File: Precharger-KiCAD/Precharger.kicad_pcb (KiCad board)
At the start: 2 copper layers, 42 parts, among them J1 Connector_Screw_Terminal_01x05, J2 Anderson_PP45_Power_RA, J3 Anderson_PP45_Power_RA, M1 Anderson_PP45_Staple_Nx2, M2 Anderson_PP45_Staple_Nx2, Q1 SQJQ480E, U1 MCP6001-OT, U2 MCP6001-OT, U3 R-78HE5.0-0.3, U4 CPC1004N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

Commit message: Continuing
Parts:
- added C6: 100nF, Capacitor_SMD:C_0805_2012Metric_Pad1.15x1.40mm_HandSolder, F.Cu at (120.6, 123.3)
- added D1: ASMB-MTB1-0A3A2, LED_SMD:LED_Avago_PLCC4_3.2x2.8mm_CW, F.Cu at (120.4, 97.9)
- added R11: 150R, Resistor_SMD:R_0805_2012Metric_Pad1.15x1.40mm_HandSolder, F.Cu at (122.5, 104.3)
- added R12: 100R, Resistor_SMD:R_0805_2012Metric_Pad1.15x1.40mm_HandSolder, F.Cu at (120.0, 104.3)
- added R13: 100R, Resistor_SMD:R_0805_2012Metric_Pad1.15x1.40mm_HandSolder, F.Cu at (117.6, 104.3)
- J1: value Connector_Screw_Terminal_01x05 -> Screw_Terminal_01x04; footprint Connector_Phoenix_MC:PhoenixContact_MCV_1,5_5-G-3.5_1x05_P3.50mm_Vertical -> TerminalBlock_Phoenix:TerminalBlock_Phoenix_PT-1,5-4-3.5-H_1x04_P3.50mm_Horizontal
- U4: moved to F.Cu
- moved R1 123.4 mm to (196.3, 73.9), turned to 270 degrees
- moved C4 106.8 mm to (189.8, 105.4)
- moved TP3 94.2 mm to (191.3, 97.8)
- moved R2 82.8 mm to (196.3, 78.2), turned to 270 degrees
- moved TP4 81.7 mm to (190.9, 133.8)
- moved U4 78.2 mm to (158.7, 61.7)
- moved JP6 75.9 mm to (160.5, 135.4)
- moved JP7 74.7 mm to (190.1, 125.7)
- moved JP5 74.0 mm to (160.5, 132.9)
- moved C1 73.8 mm to (185.1, 66.0)
- moved J3 73.8 mm to (121.3, 68.0)
- moved Q1 73.8 mm to (127.3, 76.3)
- moved A1 73.8 mm to (169.0, 97.8)
- moved C2 73.8 mm to (178.1, 69.7)
- moved C3 73.8 mm to (178.4, 73.7)
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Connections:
- A1 pad 12: Net-(A1-Pad12) -> /LED_R
- A1 pad 13: Net-(A1-Pad13) -> /LED_G
- A1 pad 14: Net-(A1-Pad14) -> /LED_B
- A1 pad 29: Net-(A1-Pad29) -> GND
- A1 pad 4: Net-(A1-Pad4) -> GND
- J1 pad 1: Net-(J1-Pad1) -> /ISO_GND
- J1 pad 2: Net-(J1-Pad2) -> /ISO_TX
- J1 pad 3: Net-(J1-Pad3) -> /ISO_RX
- J1 pad 4: Net-(J1-Pad4) -> /ISO_VCC
- JP5 pad 2: Net-(A1-Pad13) -> Net-(A1-Pad15)
- JP6 pad 2: Net-(A1-Pad14) -> Net-(A1-Pad16)
- U4 pad 3: +VSW -> Net-(R7-Pad1)
- U4 pad 4: Net-(R7-Pad1) -> +VSW
- U6 pad 5: Net-(U6-Pad5) -> /ISO_GND
- U6 pad 6: Net-(U6-Pad6) -> /ISO_TX
- U6 pad 7: Net-(U6-Pad7) -> /ISO_RX
- U6 pad 8: Net-(U6-Pad8) -> /ISO_VCC

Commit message: Close to finishing up schematic
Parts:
- added C7: 22uF, Capacitor_THT:CP_Radial_D10.0mm_P5.00mm, F.Cu at (161.1, 86.0)
- added F2: Fuse, General_Library:Fuseholder_Clip-5x20mm_Schurter_0751_0052_Horizontal_Open, F.Cu at (153.7, 87.7)
- added J5: Anderson_PP45_Power_RA, Anderson_Powerpole:Anderson_Powerpole-45A-RA-Bottom-Pair, F.Cu at (128.2, 122.7)
- added JP10: SolderJumper_2_Bridged, Jumper:SolderJumper-2_P1.3mm_Bridged2Bar_RoundedPad1.0x1.5mm, F.Cu at (132.8, 124.8)
- added JP9: SolderJumper_2_Bridged, Jumper:SolderJumper-2_P1.3mm_Bridged2Bar_RoundedPad1.0x1.5mm, F.Cu at (132.9, 132.9)
- added M3: Anderson_PP45_Staple_Nx2, Anderson_Powerpole:Anderson_Powerpole-staple-Nx2, F.Cu at (110.0, 126.7)
- added PS1: Delta_E48SC12010NRFA, General_Library:Converter_DCDC_Delta_E48SC12010_THT, F.Cu at (155.4, 111.8)
- added Q2: BSS123, Package_TO_SOT_SMD:SOT-23, F.Cu at (162.0, 105.7)
- added R14: TRIM_UP, Resistor_SMD:R_0805_2012Metric_Pad1.15x1.40mm_HandSolder, F.Cu at (114.5, 137.2)
- added R15: TRIM_UP, Resistor_SMD:R_0805_2012Metric_Pad1.15x1.40mm_HandSolder, F.Cu at (106.7, 137.1)
- added TP5: TestPoint, TestPoint:TestPoint_Keystone_5010-5014_Multipurpose, F.Cu at (212.1, 131.9)
- added TP6: TestPoint, TestPoint:TestPoint_Keystone_5010-5014_Multipurpose, F.Cu at (119.5, 137.0)
- added TP7: TestPoint, TestPoint:TestPoint_Keystone_5010-5014_Multipurpose, F.Cu at (102.5, 137.6)
- added TP8: TestPoint, TestPoint:TestPoint_Keystone_5010-5014_Multipurpose, F.Cu at (205.8, 120.3)
- moved R13 51.9 mm to (163.8, 127.9), turned to 180 degrees
- moved R12 48.6 mm to (163.8, 125.5), turned to 180 degrees
- moved D1 46.0 mm to (157.4, 125.1), turned to 270 degrees
- moved R11 45.3 mm to (163.8, 123.0), turned to 180 degrees
- moved C5 33.5 mm to (152.7, 126.2), turned to 0 degrees
- moved U6 32.7 mm to (149.1, 122.4), turned to 180 degrees
- moved J1 27.8 mm to (139.9, 134.8)
- moved C6 26.3 mm to (146.7, 126.5), turned to 0 degrees
- moved TP1 18.7 mm to (157.6, 131.7)
- moved R10 17.1 mm to (121.2, 86.4)
- moved TP2 13.2 mm to (159.4, 136.8)
- moved U5 10.3 mm to (127.8, 85.1), turned to 0 degrees
- moved A1 4.80 mm to (173.8, 97.7)
- moved JP2 4.80 mm to (167.5, 97.5)
- moved JP3 4.80 mm to (168.2, 111.8)
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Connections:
- A1 pad 10: Net-(A1-Pad10) -> (no net)
- A1 pad 11: Net-(A1-Pad11) -> /AUX_12V_ENA
- A1 pad 18: Net-(A1-Pad18) -> (no net)
- A1 pad 21: Net-(A1-Pad21) -> (no net)
- A1 pad 22: Net-(A1-Pad22) -> (no net)
- A1 pad 23: Net-(A1-Pad23) -> (no net)
- A1 pad 24: Net-(A1-Pad24) -> (no net)
- A1 pad 25: Net-(A1-Pad25) -> (no net)
- A1 pad 26: Net-(A1-Pad26) -> (no net)
- A1 pad 28: Net-(A1-Pad28) -> (no net)
- A1 pad 3: Net-(A1-Pad3) -> (no net)
- A1 pad 5: Net-(A1-Pad5) -> (no net)
- A1 pad 6: Net-(A1-Pad6) -> (no net)
- A1 pad 9: Net-(A1-Pad9) -> (no net)
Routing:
- net Net-(JP9-Pad1): track 0.00 -> 44.5 mm
- net Net-(JP10-Pad1): track 0.00 -> 43.9 mm
- net Net-(PS1-Pad6): track 0.00 -> 37.1 mm
- net +BATT: track 0.00 -> 17.9 mm
- net +VSW: track 0.00 -> 12.2 mm
- net Net-(C2-Pad1): track 0.00 -> 8.94 mm
- net /DIV_VBATT: track 0.00 -> 8.92 mm
- net Net-(C1-Pad1): track 0.00 -> 8.02 mm
- net /DIV_VSW: track 0.00 -> 7.36 mm
- net GND: track 0.00 -> 6.83 mm
- net +5V: track 0.00 -> 6.26 mm
- net Net-(Q1-PadG): track 0.00 -> 4.51 mm
- net /DIV_BUFF_VBATT: track 0.00 -> 3.92 mm
- net /DIV_BUFF_VSW: track 0.00 -> 3.74 mm
- net Net-(R4-Pad2): track 0.00 -> 2.45 mm
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- added copper zone on F.Cu, net +VSW
- added copper zone on F.Cu, net /AUX_12V_NEG
- added copper zone on F.Cu, net /AUX_12V_POS
- added copper zone on F.Cu, net /AUX_SW
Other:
- net class HV added: clearance 1, trace_width 0.25, via_dia 0.8, via_drill 0.4

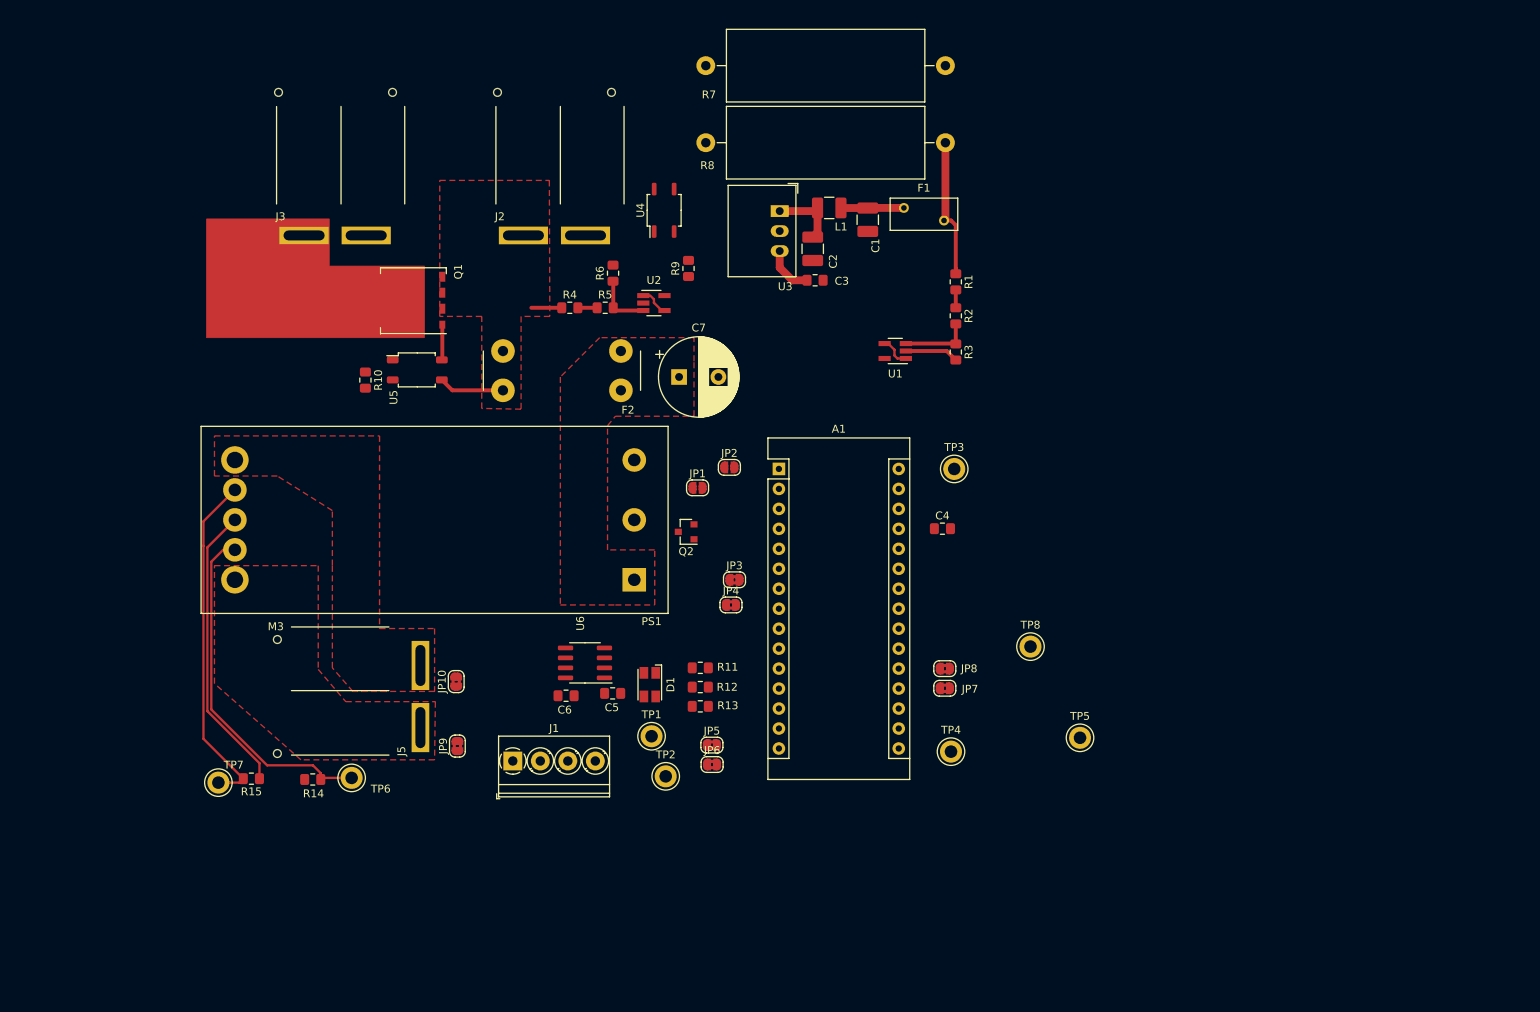
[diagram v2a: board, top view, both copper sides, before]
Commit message: Finished routing and generated fab outputs
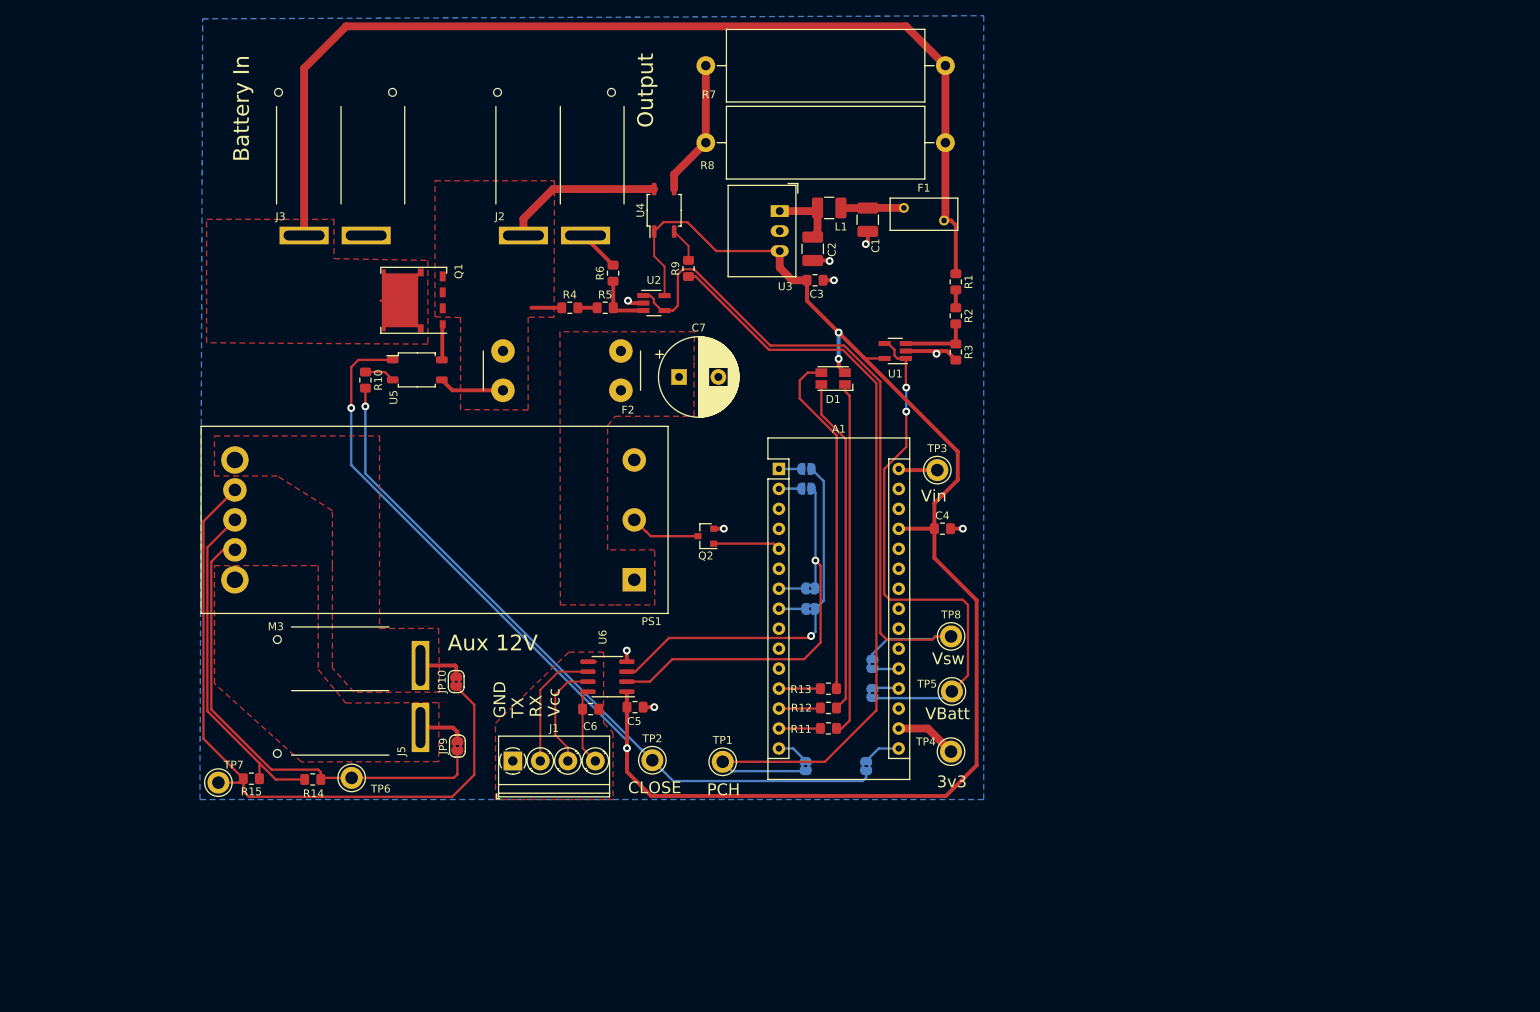
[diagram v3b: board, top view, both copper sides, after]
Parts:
- JP1, JP2, JP3, JP4, JP5, JP6, JP7, JP8: moved to B.Cu
- moved D1 45.4 mm to (180.7, 86.2), turned to 180 degrees
- moved JP6 19.6 mm to (184.9, 135.5), turned to 90 degrees
- moved R11 18.0 mm to (180.1, 130.7), turned to 0 degrees
- moved TP5 17.3 mm to (195.8, 126.0)
- moved R12 16.5 mm to (180.1, 128.1), turned to 0 degrees
- moved R13 16.5 mm to (180.1, 125.7), turned to 0 degrees
- moved JP1 13.9 mm to (177.3, 100.2), turned to 180 degrees
- moved JP5 12.2 mm to (177.2, 135.5), turned to 90 degrees
- moved TP8 10.2 mm to (195.7, 119.0)
- moved JP4 10.1 mm to (177.8, 115.5), turned to 180 degrees
- moved JP2 9.80 mm to (177.3, 97.7), turned to 180 degrees
- moved JP3 9.71 mm to (177.8, 112.9), turned to 180 degrees
- moved TP1 9.62 mm to (166.7, 134.9)
- moved JP7 9.22 mm to (185.7, 126.2), turned to 270 degrees
- moved JP8 9.22 mm to (185.7, 122.5), turned to 90 degrees
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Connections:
- A1 pad 11: /AUX_12V_ENA -> (no net)
- A1 pad 12: /LED_R -> /LED_B
- A1 pad 14: /LED_B -> /LED_R
- A1 pad 5: (no net) -> /AUX_12V_ENA
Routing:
- net +5V: track 6.26 -> 246.3 mm, vias 0 -> 4
- net +BATT: track 17.9 -> 137.3 mm
- net /~PRECHARGE: track 0.00 -> 104.4 mm
- net /~CLOSE: track 0.00 -> 91.8 mm, vias 0 -> 1
- net /DIV_BUFF_VSW: track 3.74 -> 94.7 mm
- net /DIV_BUFF_VBATT: track 3.92 -> 68.6 mm, vias 0 -> 2
- net /EXT_RX: track 0.00 -> 50.3 mm, vias 0 -> 1
- net /EXT_TX: track 0.00 -> 47.9 mm, vias 0 -> 1
- net Net-(D1-Pad1): track 0.00 -> 45.1 mm
- net Net-(JP10-Pad1): track 43.9 -> 88.5 mm
- net Net-(D1-Pad3): track 0.00 -> 44.3 mm
- net Net-(D1-Pad2): track 0.00 -> 42.9 mm
- net +VSW: track 12.2 -> 32.5 mm
- net GND: track 6.83 -> 26.0 mm, vias 0 -> 9
- net Net-(R7-Pad1): track 0.00 -> 17.4 mm
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- added copper zone on F.Cu, net +BATT
- added copper zone on F.Cu, net /ISO_GND
- added copper zone on B.Cu, net GND
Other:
- net class HV: clearance 1 -> 0.75
- board text added: "3v3"
- board text added: "Aux 12V"
- board text added: "Battery In"
- board text added: "CLOSE"
- board text added: "GND"
- board text added: "Output"
- board text added: "PCH"
- board text added: "RX"
- board text added: "TX"
- board text added: "VBatt"
- board text added: "Vcc"
- board text added: "Vin"
- board text added: "Vsw"
